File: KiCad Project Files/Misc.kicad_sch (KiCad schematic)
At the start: 19 parts, among them J2 SWD, U5 74AHCT1G125

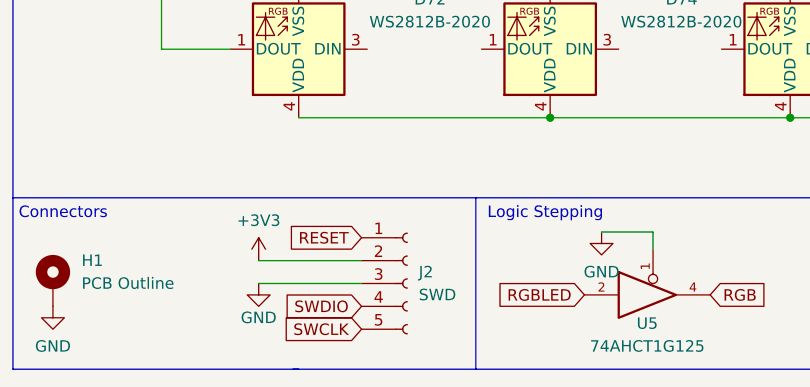
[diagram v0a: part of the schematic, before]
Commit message: Add files via upload
updated schematics
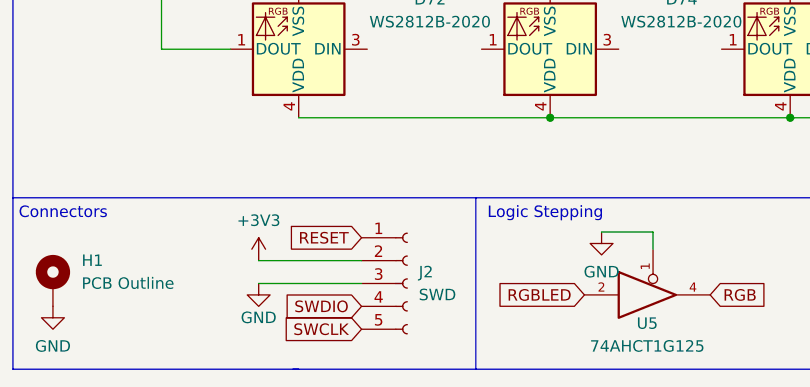
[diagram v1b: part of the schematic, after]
